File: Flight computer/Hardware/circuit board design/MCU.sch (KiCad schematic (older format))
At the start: 31 parts, among them J1 Conn_01x04, U11 ATSAML21J18B-AUT, U7 W74M64FV, Y3 16MHz

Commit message: added pull down resistor to arm switch pin to prevent it from floating and accidentally fireing
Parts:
- added R4: 1K, Resistor_SMD:R_0603_1608Metric, symbol Device:R
- gave numbers to parts that had none: 1
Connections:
- wire segments 174 -> 175
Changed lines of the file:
@@
 	8700 3750 8800 3750
 Wire Wire Line
-	8800 3750 8800 4100
+	8800 3750 8800 3900
 Connection ~ 8800 3750
 Wire Wire Line
 	8800 3750 8900 3750
 $Comp
-L power:GND #PWR?
+L power:GND #PWR017
 U 1 1 5D83136F
-P 8800 4100
-F 0 "#PWR?" H 8800 3850 50  0001 C CNN
-F 1 "GND" H 8805 3927 50  0000 C CNN
-F 2 "" H 8800 4100 50  0001 C CNN
-F 3 "" H 8800 4100 50  0001 C CNN
-	1    8800 4100
+P 8800 4250
+F 0 "#PWR017" H 8800 4000 50  0001 C CNN
+F 1 "GND" H 8805 4077 50  0000 C CNN
+F 2 "" H 8800 4250 50  0001 C CNN
+F 3 "" H 8800 4250 50  0001 C CNN
+	1    8800 4250
 	1    0    0    -1
 $EndComp
 $Comp
-L Switch:SW_SPST SW?
+L Switch:SW_SPST SW1
 U 1 1 5D832A6E
 P 9100 3750
-F 0 "SW?" H 9100 3985 50  0000 C CNN
+F 0 "SW1" H 9100 3985 50  0000 C CNN
 F 1 "SW_SPST" H 9100 3894 50  0000 C CNN
 F 2 "" H 9100 3750 50  0001 C CNN
@@
 $EndComp
 $Comp
-L power:+3.3V #PWR?
+L power:+3.3V #PWR029
 U 1 1 5D832E28
 P 9450 3350
-F 0 "#PWR?" H 9450 3200 50  0001 C CNN
+F 0 "#PWR029" H 9450 3200 50  0001 C CNN
 F 1 "+3.3V" H 9400 3500 50  0000 C CNN
 F 2 "" H 9450 3350 50  0001 C CNN
@@
 Wire Notes Line
 	8200 4500 11050 4500
-Text Notes 8200 4800 0    50   ~ 0
+Text Notes 8300 3400 0    50   ~ 0
 Switch to arm pyro \nand go into ready to \nfire mode
+$Comp
+L Device:R R4
+U 1 1 5D854BB0
+P 8800 4050
+F 0 "R4" H 8870 4096 50  0000 L CNN
+F 1 "1K" H 8870 4005 50  0000 L CNN
+F 2 "Resistor_SMD:R_0603_1608Metric" V 8730 4050 50  0001 C CNN
+F 3 "~" H 8800 4050 50  0001 C CNN
+	1    8800 4050
+	-1   0    0    -1
+$EndComp
+Wire Wire Line
+	8800 4200 8800 4250
 $EndSCHEMATC

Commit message: moved reset pin to programming pin header
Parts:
- J1: value Conn_01x04 -> Conn_01x05; symbol Connector_Generic:Conn_01x04 -> Connector_Generic:Conn_01x05
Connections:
- wire segments 175 -> 178
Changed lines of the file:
@@
 	1    0    0    -1
-$EndComp
-$Comp
-L Connector_Generic:Conn_01x04 J1
-U 1 1 5D3DC905
-P 1250 4450
-F 0 "J1" H 1330 4442 50  0000 L CNN
-F 1 "Conn_01x04" H 1330 4351 50  0000 L CNN
-F 2 "Connector_PinHeader_2.54mm:PinHeader_1x05_P2.54mm_Vertical" H 1250 4450 50  0001 C CNN
-F 3 "~" H 1250 4450 50  0001 C CNN
-	1    1250 4450
-	-1   0    0    -1
 $EndComp
 Wire Wire Line
@@
 	3900 4050 2800 4050
 $Comp
-L Device:R R12
-U 1 1 5D70BAB2
-P 4450 6250
-F 0 "R12" H 4520 6296 50  0000 L CNN
-F 1 "1K" H 4520 6205 50  0000 L CNN
-F 2 "Resistor_SMD:R_0603_1608Metric" V 4380 6250 50  0001 C CNN
-F 3 "~" H 4450 6250 50  0001 C CNN
-	1    4450 6250
-	-1   0    0    -1
-$EndComp
-$Comp
 L Device:C C89
 U 1 1 5D70C5B6
@@
 Wire Wire Line
 	4450 6550 4450 6400
-Wire Wire Line
-	4450 6100 4450 5950
 Wire Wire Line
 	4450 7000 4450 7100
@@
 	1    0    0    -1
 $EndComp
-$Comp
-L power:+3.3V #PWR018
-U 1 1 5D6BAA49
-P 4450 5950
-F 0 "#PWR018" H 4450 5800 50  0001 C CNN
-F 1 "+3.3V" H 4465 6123 50  0000 C CNN
-F 2 "" H 4450 5950 50  0001 C CNN
-F 3 "" H 4450 5950 50  0001 C CNN
-	1    4450 5950
-	1    0    0    -1
-$EndComp
 Wire Notes Line
 	550  3200 2550 3200
@@
 Wire Notes Line
 	550  5900 550  3200
-Text Notes 1050 5800 0    50   ~ 0
+Text Notes 700  3300 0    50   ~ 0
 Programming interface\n
 $Comp
@@
 Wire Wire Line
 	8800 4200 8800 4250
+$Comp
+L Connector_Generic:Conn_01x05 J1
+U 1 1 5D3DC905
+P 1250 4550
+F 0 "J1" H 1330 4542 50  0000 L CNN
+F 1 "Conn_01x05" H 1330 4451 50  0000 L CNN
+F 2 "Connector_PinHeader_2.54mm:PinHeader_1x05_P2.54mm_Vertical" H 1250 4550 50  0001 C CNN
+F 3 "~" H 1250 4550 50  0001 C CNN
+	1    1250 4550
+	-1   0    0    -1
+$EndComp
+Wire Wire Line
+	1450 4750 1500 4750
+Wire Wire Line
+	1500 4750 1500 5800
+Wire Wire Line
+	1500 5800 4450 5800
+$Comp
+L Device:R R12
+U 1 1 5D70BAB2
+P 4450 6250
+F 0 "R12" H 4520 6296 50  0000 L CNN
+F 1 "1K" H 4520 6205 50  0000 L CNN
+F 2 "Resistor_SMD:R_0603_1608Metric" V 4380 6250 50  0001 C CNN
+F 3 "~" H 4450 6250 50  0001 C CNN
+	1    4450 6250
+	-1   0    0    -1
+$EndComp
+Wire Wire Line
+	4450 5800 4450 6100
 $EndSCHEMATC

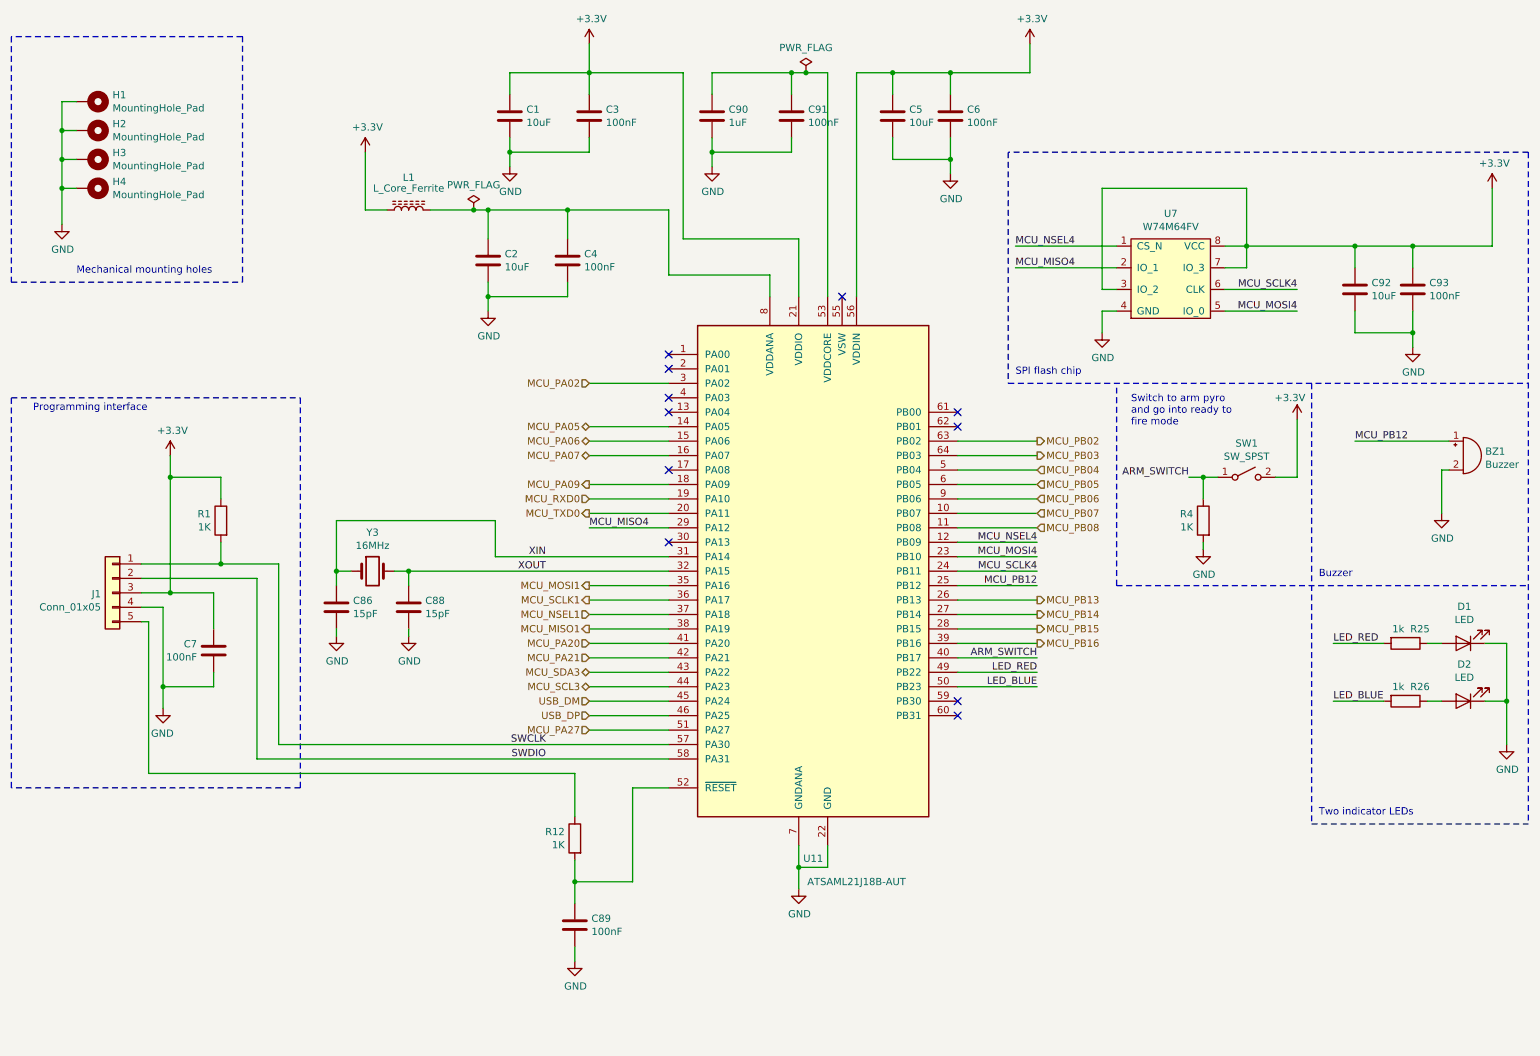
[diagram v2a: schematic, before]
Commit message: standardised the symbol for the Johanson RF front end
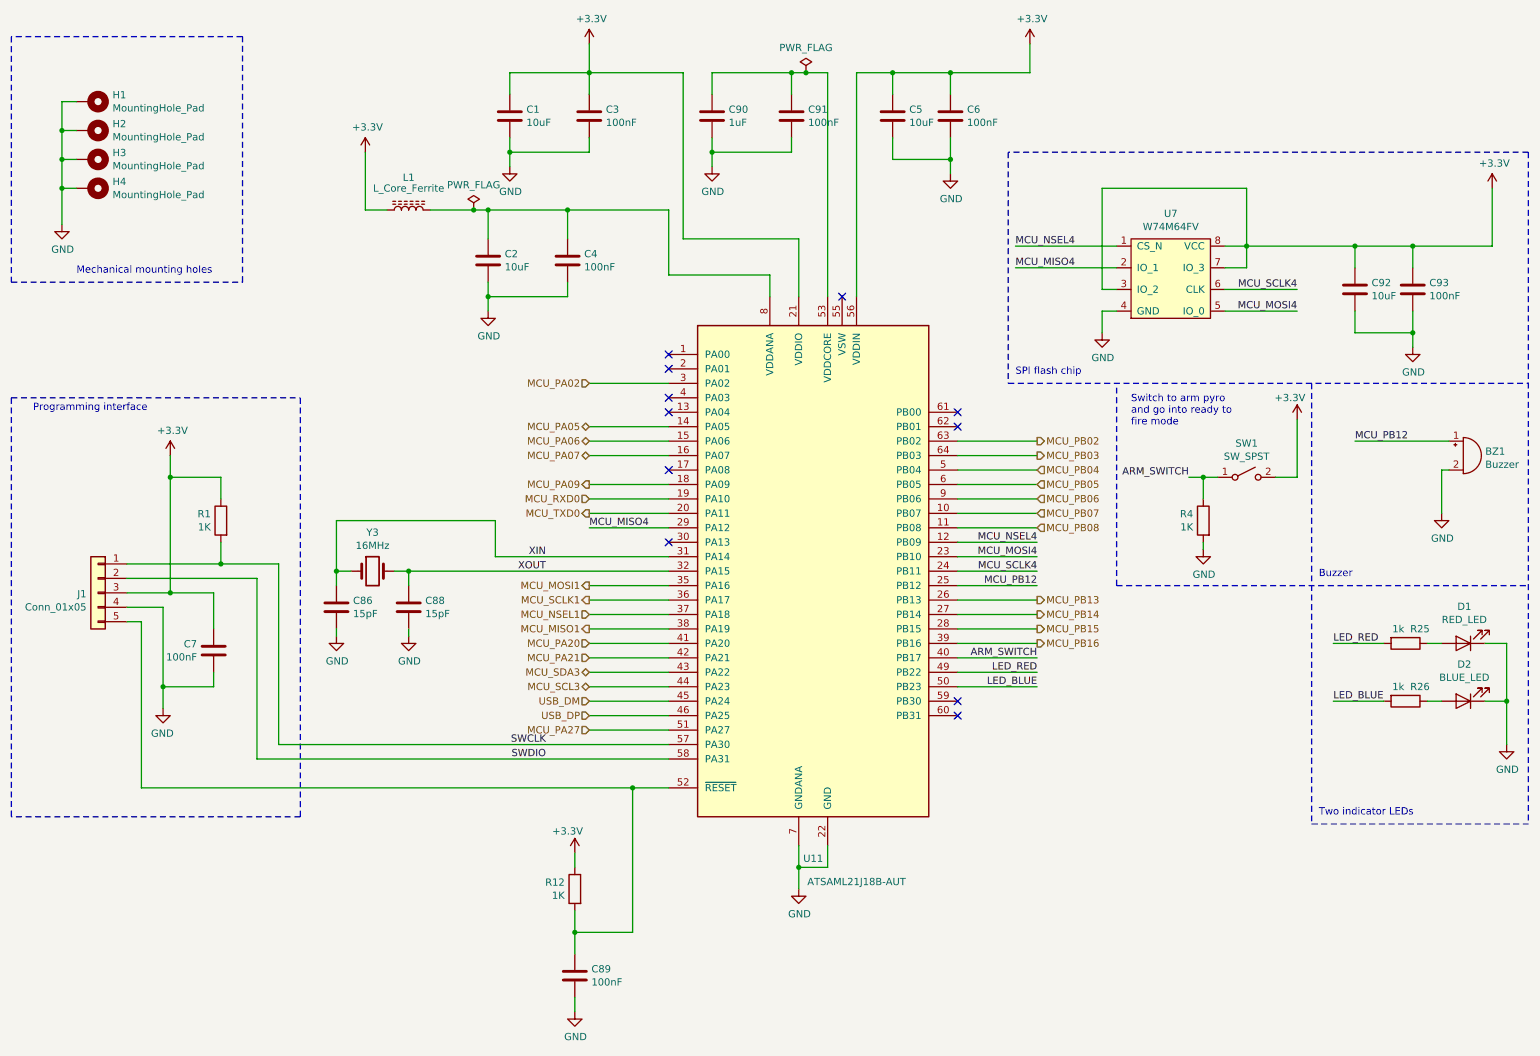
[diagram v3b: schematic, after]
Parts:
- D1: value LED -> RED_LED
- D2: value LED -> BLUE_LED
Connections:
- net +3V3: now also R12.1
- net at J1.5 (Pin_5): now also C89.1, R12.2, U11.52 (~RESET); no longer R12.1
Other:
- moved on the sheet: C89, J1, R12
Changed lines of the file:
@@
 $EndComp
 Wire Wire Line
-	1650 4550 1450 4550
-Wire Wire Line
-	1600 4650 1450 4650
+	1650 4550 1350 4550
+Wire Wire Line
+	1600 4650 1350 4650
 $Comp
 L Device:R R1
@@
 	2000 4200 2000 4350
 Wire Wire Line
-	2000 4350 1450 4350
+	2000 4350 1350 4350
 Wire Wire Line
 	1950 4550 1650 4550
@@
 	4550 950  4550 750
 Wire Wire Line
-	4850 6550 4850 5900
-Wire Wire Line
 	4850 5900 5100 5900
 Wire Wire Line
@@
 Connection ~ 2000 4350
 Wire Wire Line
-	2250 4450 1450 4450
+	2250 4450 1350 4450
 $Comp
 L Device:Crystal Y3
@@
 	2800 4400 2800 4050
 Connection ~ 2800 4400
-Wire Wire Line
-	3900 4300 3900 4050
-Wire Wire Line
-	3900 4050 2800 4050
 $Comp
 L Device:C C89
 U 1 1 5D70C5B6
-P 4450 6850
-F 0 "C89" H 4565 6896 50  0000 L CNN
-F 1 "100nF" H 4565 6805 50  0000 L CNN
-F 2 "Capacitor_SMD:C_0603_1608Metric" H 4488 6700 50  0001 C CNN
-F 3 "~" H 4450 6850 50  0001 C CNN
-	1    4450 6850
+P 4450 7200
+F 0 "C89" H 4565 7246 50  0000 L CNN
+F 1 "100nF" H 4565 7155 50  0000 L CNN
+F 2 "Capacitor_SMD:C_0603_1608Metric" H 4488 7050 50  0001 C CNN
+F 3 "~" H 4450 7200 50  0001 C CNN
+	1    4450 7200
 	1    0    0    -1
 $EndComp
@@
 L power:GND #PWR087
 U 1 1 5D70CF68
-P 4450 7100
-F 0 "#PWR087" H 4450 6850 50  0001 C CNN
-F 1 "GND" H 4455 6927 50  0000 C CNN
-F 2 "" H 4450 7100 50  0001 C CNN
-F 3 "" H 4450 7100 50  0001 C CNN
-	1    4450 7100
-	1    0    0    -1
-$EndComp
-Wire Wire Line
-	4450 6700 4450 6550
-Wire Wire Line
-	4850 6550 4450 6550
-Connection ~ 4450 6550
-Wire Wire Line
-	4450 6550 4450 6400
-Wire Wire Line
-	4450 7000 4450 7100
+P 4450 7450
+F 0 "#PWR087" H 4450 7200 50  0001 C CNN
+F 1 "GND" H 4455 7277 50  0000 C CNN
+F 2 "" H 4450 7450 50  0001 C CNN
+F 3 "" H 4450 7450 50  0001 C CNN
+	1    4450 7450
+	1    0    0    -1
+$EndComp
+Wire Wire Line
+	4450 7350 4450 7450
 Wire Wire Line
 	5100 5700 2250 5700
@@
 	550  3200 2550 3200
 Wire Notes Line
-	2550 3200 2550 5900
-Wire Notes Line
-	2550 5900 550  5900
-Wire Notes Line
-	550  5900 550  3200
+	2550 6100 550  6100
 Text Notes 700  3300 0    50   ~ 0
 Programming interface\n
@@
 Wire Wire Line
 	3300 4400 5100 4400
-Wire Wire Line
-	3900 4300 5100 4300
 NoConn ~ 7100 5400
 NoConn ~ 7100 5300
@@
 P 10600 5300
 F 0 "D2" H 10593 5045 50  0000 C CNN
-F 1 "LED" H 10593 5136 50  0000 C CNN
+F 1 "BLUE_LED" H 10593 5136 50  0000 C CNN
 F 2 "LED_SMD:LED_0603_1608Metric" H 10600 5300 50  0001 C CNN
 F 3 "~" H 10600 5300 50  0001 C CNN
@@
 P 10600 4900
 F 0 "D1" H 10593 4645 50  0000 C CNN
-F 1 "LED" H 10593 4736 50  0000 C CNN
+F 1 "RED_LED" H 10593 4736 50  0000 C CNN
 F 2 "LED_SMD:LED_0603_1608Metric" H 10600 4900 50  0001 C CNN
 F 3 "~" H 10600 4900 50  0001 C CNN
@@
 L Connector_Generic:Conn_01x05 J1
 U 1 1 5D3DC905
-P 1250 4550
-F 0 "J1" H 1330 4542 50  0000 L CNN
-F 1 "Conn_01x05" H 1330 4451 50  0000 L CNN
-F 2 "Connector_PinHeader_2.54mm:PinHeader_1x05_P2.54mm_Vertical" H 1250 4550 50  0001 C CNN
-F 3 "~" H 1250 4550 50  0001 C CNN
-	1    1250 4550
+P 1150 4550
+F 0 "J1" H 1230 4542 50  0000 L CNN
+F 1 "Conn_01x05" H 1230 4451 50  0000 L CNN
+F 2 "Connector_PinHeader_2.54mm:PinHeader_1x05_P2.54mm_Vertical" H 1150 4550 50  0001 C CNN
+F 3 "~" H 1150 4550 50  0001 C CNN
+	1    1150 4550
 	-1   0    0    -1
 $EndComp
 Wire Wire Line
-	1450 4750 1500 4750
-Wire Wire Line
-	1500 4750 1500 5800
-Wire Wire Line
-	1500 5800 4450 5800
+	1350 4750 1450 4750
 $Comp
 L Device:R R12
 U 1 1 5D70BAB2
-P 4450 6250
-F 0 "R12" H 4520 6296 50  0000 L CNN
-F 1 "1K" H 4520 6205 50  0000 L CNN
-F 2 "Resistor_SMD:R_0603_1608Metric" V 4380 6250 50  0001 C CNN
-F 3 "~" H 4450 6250 50  0001 C CNN
-	1    4450 6250
+P 4450 6600
+F 0 "R12" H 4520 6646 50  0000 L CNN
+F 1 "1K" H 4520 6555 50  0000 L CNN
+F 2 "Resistor_SMD:R_0603_1608Metric" V 4380 6600 50  0001 C CNN
+F 3 "~" H 4450 6600 50  0001 C CNN
+	1    4450 6600
 	-1   0    0    -1
 $EndComp
 Wire Wire Line
-	4450 5800 4450 6100
+	4450 6350 4450 6450
+$Comp
+L power:+3.3V #PWR?
+U 1 1 5D7A484D
+P 4450 6350
+F 0 "#PWR?" H 4450 6200 50  0001 C CNN
+F 1 "+3.3V" H 4400 6500 50  0000 C CNN
+F 2 "" H 4450 6350 50  0001 C CNN
+F 3 "" H 4450 6350 50  0001 C CNN
+	1    4450 6350
+	1    0    0    -1
+$EndComp
+Wire Wire Line
+	4450 6750 4450 6900
+Wire Wire Line
+	4450 6900 4850 6900
+Wire Wire Line
+	4850 5900 4850 6900
+Connection ~ 4450 6900
+Wire Wire Line
+	4450 6900 4450 7050
+Wire Wire Line
+	4850 5900 1450 5900
+Wire Wire Line
+	1450 4750 1450 5900
+Connection ~ 4850 5900
+Wire Notes Line
+	2550 6100 2550 3200
+Wire Notes Line
+	550  3200 550  6100
+Wire Wire Line
+	3900 4050 2800 4050
+Wire Wire Line
+	3900 4300 5100 4300
+Wire Wire Line
+	3900 4300 3900 4050
 $EndSCHEMATC

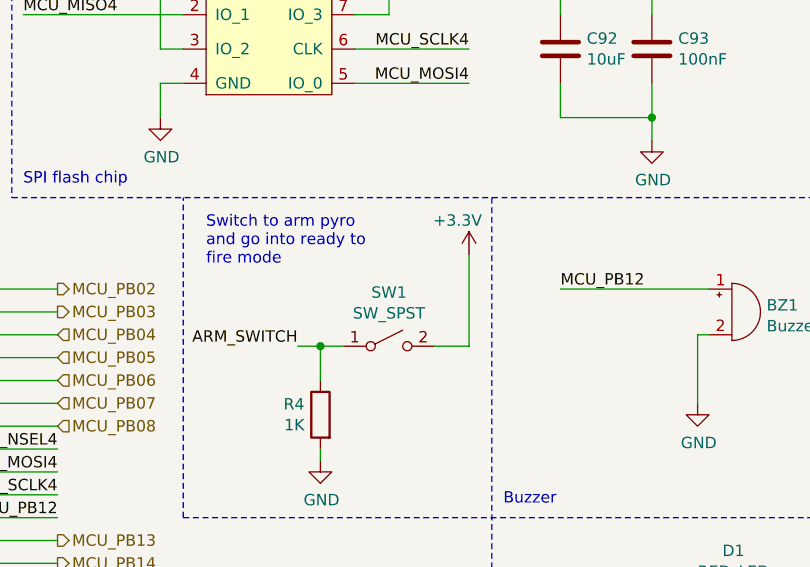
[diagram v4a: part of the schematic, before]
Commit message: added the arming switch. Changed foot print of lipo connector to JST
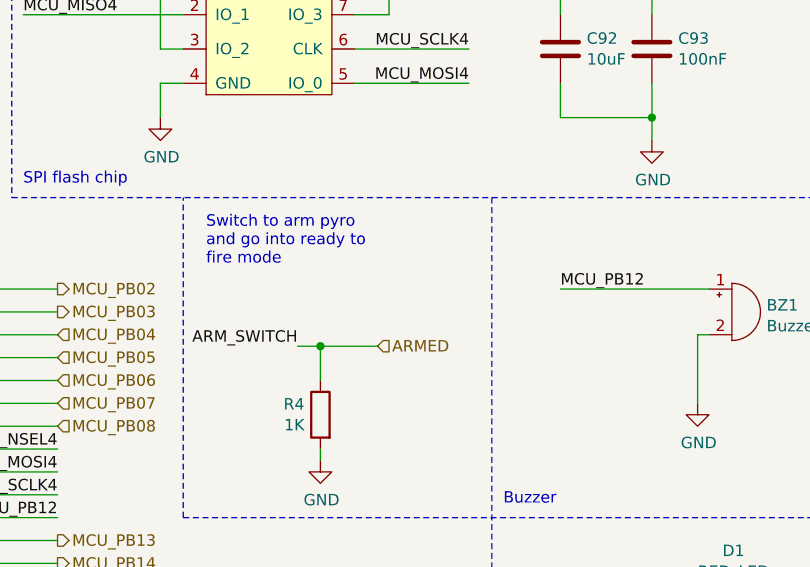
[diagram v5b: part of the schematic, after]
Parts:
- removed SW1: SW_SPST, symbol Switch:SW_SPST
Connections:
- net ARM_SWITCH renamed ARMED
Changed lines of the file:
@@
 Wire Notes Line
 	9550 6150 11050 6150
-Wire Notes Line
-	9550 3100 9550 6150
 Text Notes 9600 6100 0    50   ~ 0
 Two indicator LEDs
@@
 Connection ~ 8800 3750
 Wire Wire Line
-	8800 3750 8900 3750
+	8800 3750 9050 3750
 $Comp
 L power:GND #PWR017
@@
 	1    0    0    -1
 $EndComp
-$Comp
-L Switch:SW_SPST SW1
-U 1 1 5D832A6E
-P 9100 3750
-F 0 "SW1" H 9100 3985 50  0000 C CNN
-F 1 "SW_SPST" H 9100 3894 50  0000 C CNN
-F 2 "" H 9100 3750 50  0001 C CNN
-F 3 "~" H 9100 3750 50  0001 C CNN
-	1    9100 3750
-	1    0    0    -1
-$EndComp
-$Comp
-L power:+3.3V #PWR029
-U 1 1 5D832E28
-P 9450 3350
-F 0 "#PWR029" H 9450 3200 50  0001 C CNN
-F 1 "+3.3V" H 9400 3500 50  0000 C CNN
-F 2 "" H 9450 3350 50  0001 C CNN
-F 3 "" H 9450 3350 50  0001 C CNN
-	1    9450 3350
-	1    0    0    -1
-$EndComp
-Wire Wire Line
-	9450 3750 9450 3350
-Wire Wire Line
-	9300 3750 9450 3750
 Wire Notes Line
 	8200 4500 8200 3100
@@
 Wire Wire Line
 	3900 4300 3900 4050
+Wire Notes Line
+	9550 3100 9550 6150
+Text HLabel 9050 3750 2    50   Input ~ 0
+ARMED
 $EndSCHEMATC

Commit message: tried routing first round
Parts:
- Y3: symbol Device:Crystal -> Device:Crystal_GND24
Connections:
- net GND: now also Y3.2, Y3.4
- net XOUT: now also Y3.3; no longer Y3.2
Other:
- moved on the sheet: C88

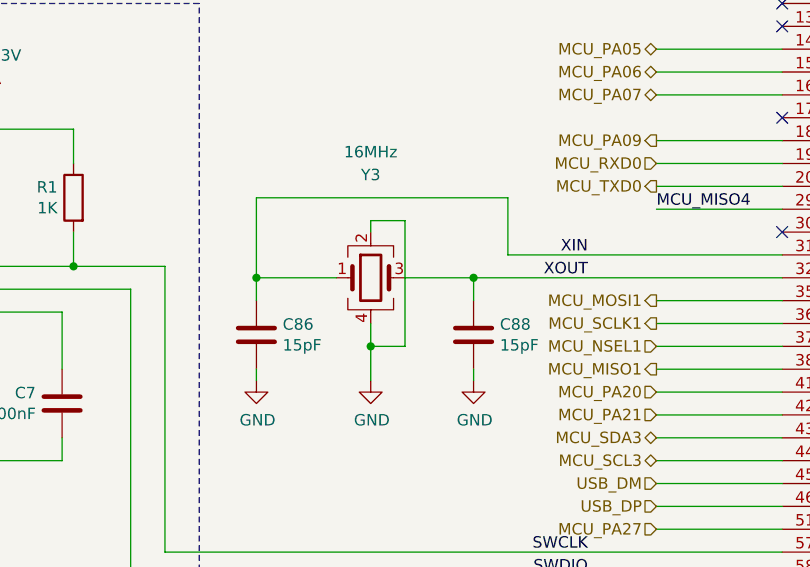
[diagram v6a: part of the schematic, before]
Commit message: put in the Yageo 434 antenna
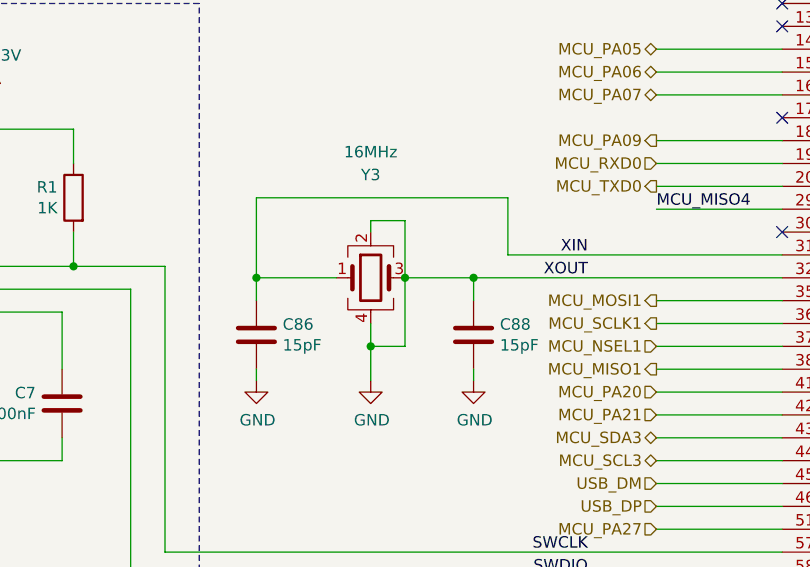
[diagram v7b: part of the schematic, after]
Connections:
- net XOUT is gone; now on net GND: C88.1, U11.32 (PA15), Y3.3
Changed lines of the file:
@@
 Wire Wire Line
 	5100 4800 4550 4800
-Text HLabel 4550 4500 0    50   Output ~ 0
-MCU_MOSI1
-Text HLabel 4550 4600 0    50   Output ~ 0
-MCU_SCLK1
-Text HLabel 4550 4700 0    50   Input ~ 0
-MCU_NSEL1
-Text HLabel 4550 4800 0    50   Output ~ 0
-MCU_MISO1
 Wire Wire Line
 	5100 5200 4550 5200
@@
 	5100 4500 4550 4500
 NoConn ~ 7100 5400
-NoConn ~ 7100 5300
 Wire Notes Line
 	7450 1500 7450 3100
@@
 Wire Wire Line
 	9850 3500 10500 3500
-Text Label 7650 4500 2    50   ~ 0
-MCU_PB12
 Text Notes 9600 4450 0    50   ~ 0
 Buzzer\n
@@
 	1    0    0    -1
 $EndComp
+NoConn ~ 7100 5300
+Text Label 7650 4500 2    50   ~ 0
+MCU_PB12
+Text HLabel 4550 4800 0    50   Output ~ 0
+MCU_MISO1
+Text HLabel 4550 4700 0    50   Input ~ 0
+MCU_NSEL1
+Text HLabel 4550 4600 0    50   Output ~ 0
+MCU_SCLK1
+Text HLabel 4550 4500 0    50   Output ~ 0
+MCU_MOSI1
+Wire Wire Line
+	3300 4200 3300 4150
+Wire Wire Line
+	3300 4150 3450 4150
+Wire Wire Line
+	3450 4700 3300 4700
+Wire Wire Line
+	3450 4150 3450 4400
+Wire Wire Line
+	3450 4400 3450 4700
+Connection ~ 3450 4400
 Wire Wire Line
 	3300 4600 3300 4700
 Wire Wire Line
-	3300 4200 3300 4150
-Wire Wire Line
-	3300 4150 3450 4150
-Wire Wire Line
-	3450 4700 3300 4700
+	3300 4700 3300 4850
 Connection ~ 3300 4700
-Wire Wire Line
-	3300 4700 3300 4850
-Wire Wire Line
-	3450 4150 3450 4700
 $EndSCHEMATC
